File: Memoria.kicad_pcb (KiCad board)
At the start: 2 copper layers, 242.9 x 96.6 mm, 140 parts, among them J1 RGB Breakout, J2 Hull LED Breakout, U1 PRTR5V0U2X, U2 ATmega32U4-MUR, Y1 16MHz

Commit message: cleanup
moved termination resistors closer to mcu, added hotswap sockets to bom, updated readme.md
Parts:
- moved R6 88.3 mm to (132.2, 82.5), turned to -90 degrees
- moved R7 85.5 mm to (130.2, 82.5), turned to -90 degrees
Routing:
- net D+: track 22.2 -> 154.7 mm
- net D-: track 17.9 -> 149.5 mm
- net Net-(R7-Pad2): track 153.7 -> 22.8 mm
- net Net-(R6-Pad2): track 151.7 -> 21.8 mm
- net col5: track 93.3 -> 98.9 mm
- net rgbLED: track 107.1 -> 105.7 mm
- net +5V: track 403.9 -> 402.6 mm
- net row3: track 225.9 -> 225.1 mm
- net col6: track 83.8 -> 83.0 mm
- net GND: track 331.4 -> 330.7 mm

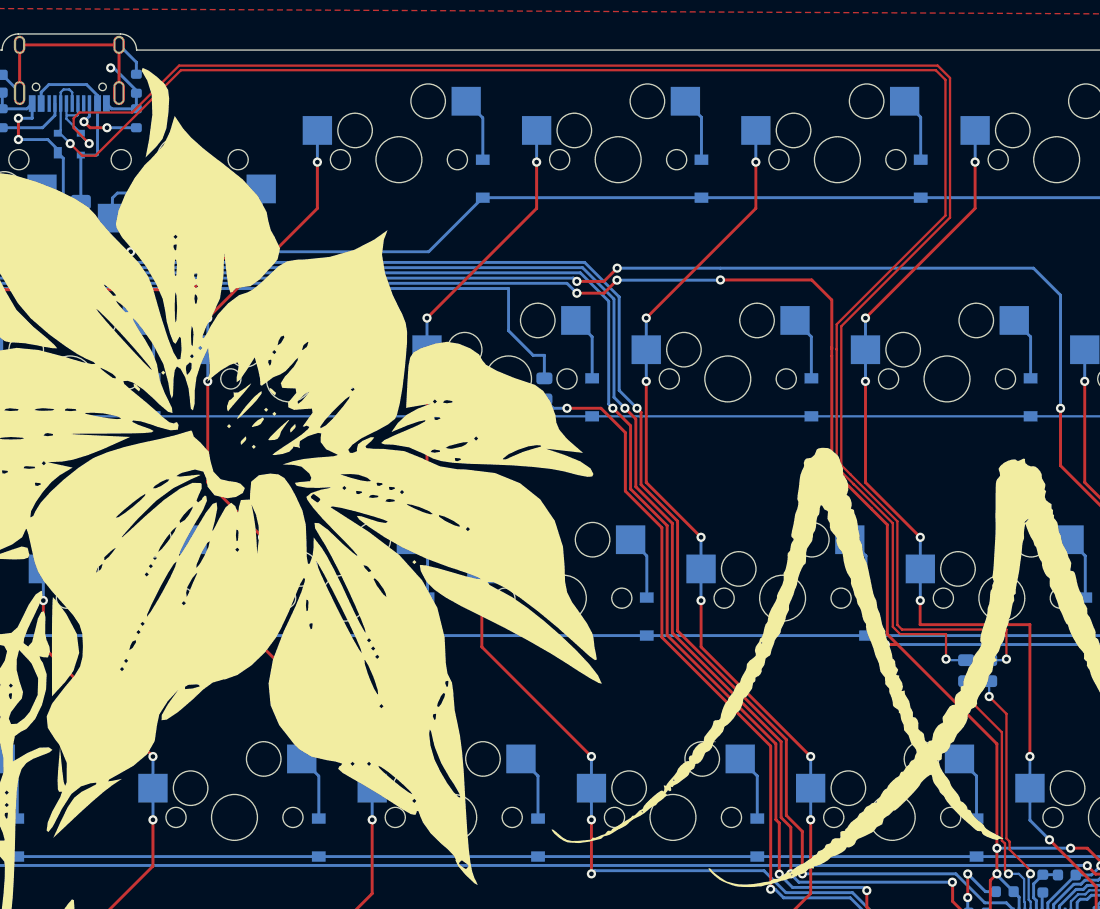
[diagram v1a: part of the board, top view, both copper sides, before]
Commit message: skewed data line length
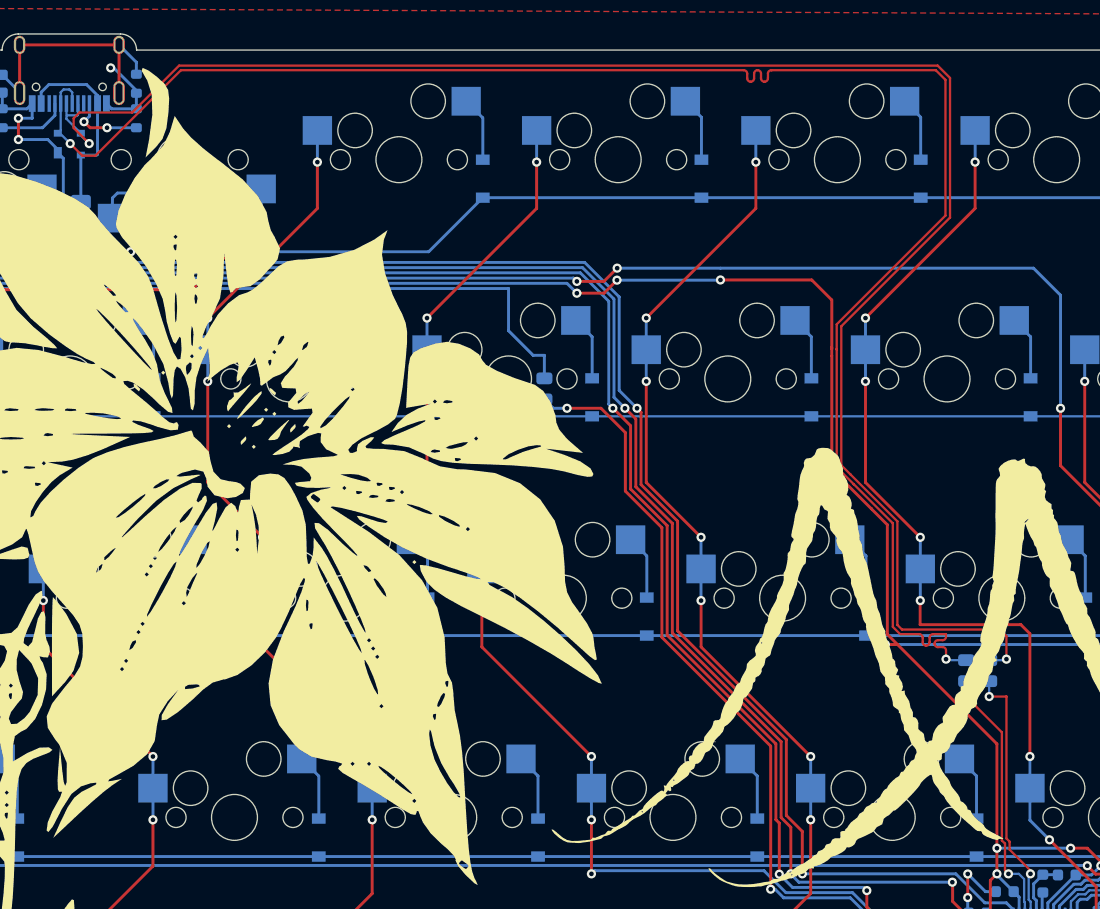
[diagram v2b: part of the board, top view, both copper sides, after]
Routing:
- net D-: track 149.5 -> 155.2 mm
- net Net-(R6-Pad2): track 21.8 -> 22.7 mm
